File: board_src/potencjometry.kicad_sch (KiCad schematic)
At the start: 8 parts, among them J13 Conn_01x03, Q1 NPN

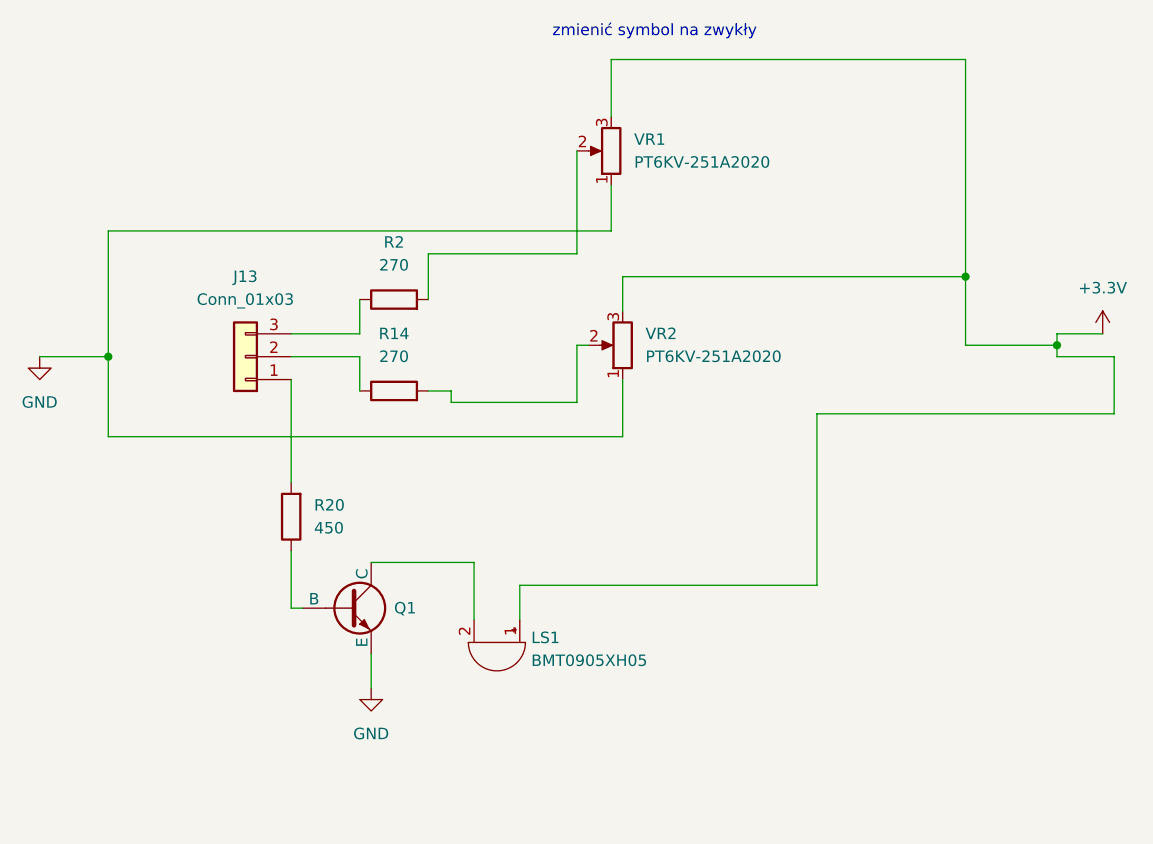
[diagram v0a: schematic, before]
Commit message: Poprawki w schematach. Rozpoczęte korekty płytki
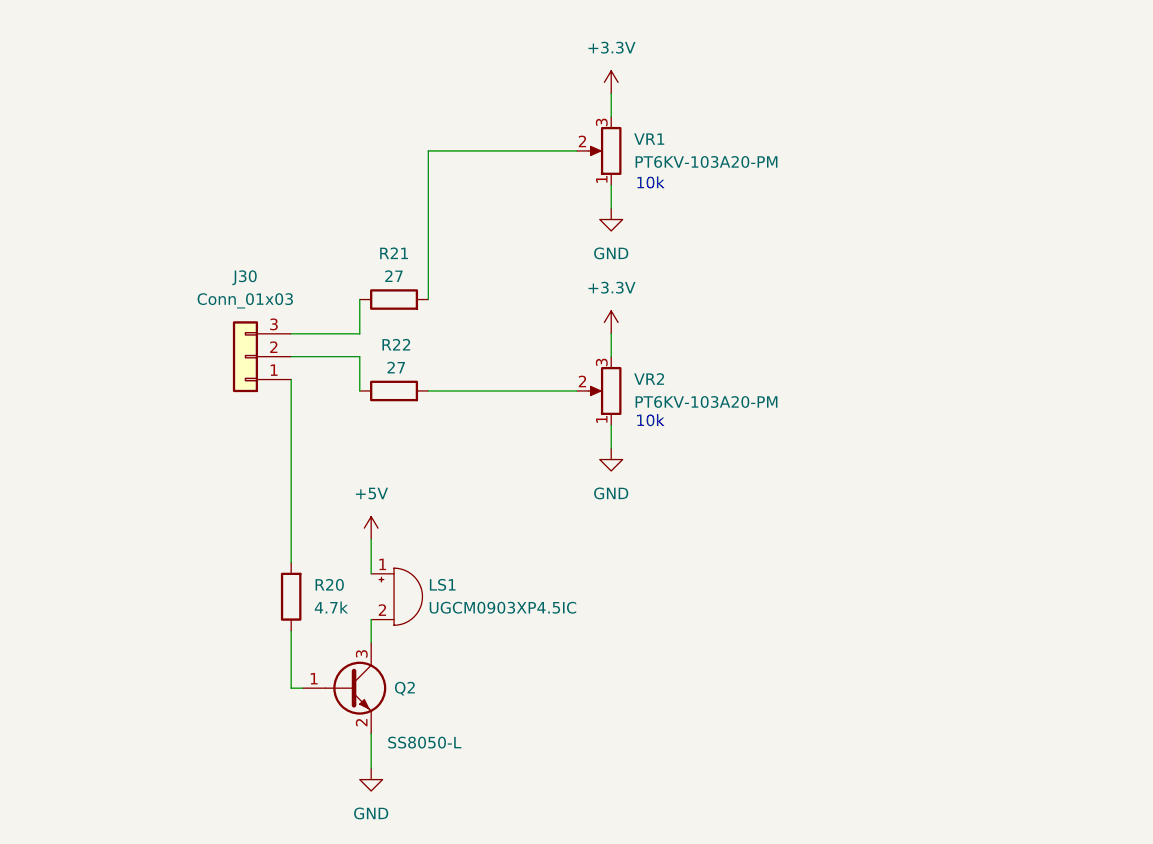
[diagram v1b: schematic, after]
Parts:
- J30: renamed from J13; footprint Connector_PinHeader_2.54mm:PinHeader_1x03_P2.54mm_Vertical -> Connector_PinHeader_2.54mm:PinHeader_1x10_P2.54mm_Vertical
- LS1: value BMT0905XH05 -> UGCM0903XP4.5IC
- Q2: renamed from Q1; value NPN -> SS8050-L; footprint Package_TO_SOT_SMD:SOT-23 -> Package_TO_SOT_SMD:SOT-23_Handsoldering; symbol Simulation_SPICE:NPN -> Transistor_BJT:SS8050
- R20: value 450 -> 4.7k; footprint Resistor_SMD:R_0603_1608Metric -> Resistor_SMD:R_0603_1608Metric_Pad0.98x0.95mm_HandSolder
- R21: renamed from R2; value 270 -> 27; footprint Resistor_SMD:R_0603_1608Metric -> Resistor_SMD:R_0603_1608Metric_Pad0.98x0.95mm_HandSolder
- R22: renamed from R14; value 270 -> 27; footprint Resistor_SMD:R_0603_1608Metric -> Resistor_SMD:R_0603_1608Metric_Pad0.98x0.95mm_HandSolder
- VR1, VR2: value PT6KV-251A2020 -> PT6KV-103A20-PM
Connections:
- net +3.3V: no longer LS1.1 (+)
- net GND: now also Q2.2 (E); no longer Q2.3 (E)
- net at R20.1: now also Q2.1 (B); no longer Q2.2 (B)
- net at LS1.2 (-): now also Q2.3 (C); no longer Q2.1 (C)
- new net +5V: LS1.1 (+)
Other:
- note added: "10k"
- note removed: "zmienić symbol na zwykły"
- moved on the sheet: LS1, R20, VR2

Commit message: Wprowadzono usprawnienia i poprawki. Wersja ostateczna, wysłana do JLCPCB.
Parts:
- J30: footprint Connector_PinHeader_2.54mm:PinHeader_1x10_P2.54mm_Vertical -> Connector_PinHeader_2.54mm:PinHeader_1x03_P2.54mm_Vertical
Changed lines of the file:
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@@
 			)
 		)
-		(property "Footprint" "Connector_PinHeader_2.54mm:PinHeader_1x10_P2.54mm_Vertical"
+		(property "Footprint" "Connector_PinHeader_2.54mm:PinHeader_1x03_P2.54mm_Vertical"
 			(at 76.2 88.9 0)
 			(effects
